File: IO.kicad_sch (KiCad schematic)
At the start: 12 parts, among them J2 Conn_Coaxial, J3 Conn_Coaxial, U6 ADG902BRMZ

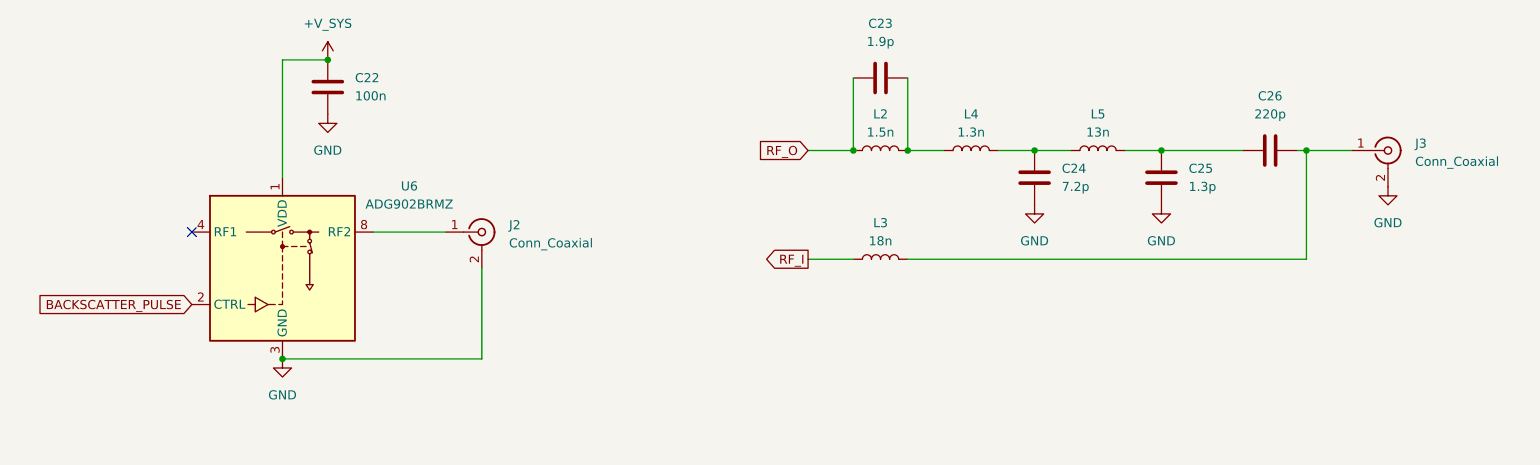
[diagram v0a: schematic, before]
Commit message: add IO ports, begin layout
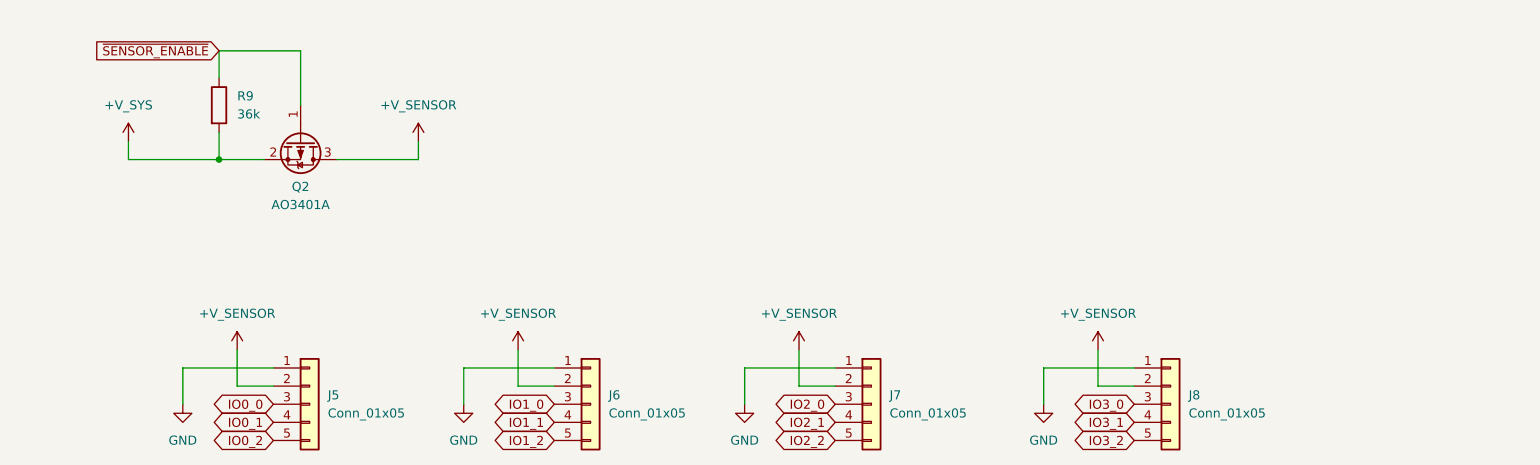
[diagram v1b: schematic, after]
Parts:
- removed C22: 100n, Capacitor_SMD:C_0603_1608Metric_Pad1.08x0.95mm_HandSolder, symbol Device:C
- removed C23: 1.9p, Capacitor_SMD:C_0603_1608Metric_Pad1.08x0.95mm_HandSolder, symbol Device:C
- removed C24: 7.2p, Capacitor_SMD:C_0603_1608Metric_Pad1.08x0.95mm_HandSolder, symbol Device:C
- removed C25: 1.3p, Capacitor_SMD:C_0603_1608Metric_Pad1.08x0.95mm_HandSolder, symbol Device:C
- removed C26: 220p, Capacitor_SMD:C_0603_1608Metric_Pad1.08x0.95mm_HandSolder, symbol Device:C
- removed J2, J3: Conn_Coaxial, Connector_Coaxial:SMA_Molex_73251-2200_Horizontal, symbol Connector:Conn_Coaxial
- removed L2: 1.5n, Inductor_SMD:L_0603_1608Metric_Pad1.05x0.95mm_HandSolder, symbol Device:L
- removed L3: 18n, Inductor_SMD:L_0603_1608Metric_Pad1.05x0.95mm_HandSolder, symbol Device:L
- removed L4: 1.3n, Inductor_SMD:L_0603_1608Metric_Pad1.05x0.95mm_HandSolder, symbol Device:L
- removed L5: 13n, Inductor_SMD:L_0603_1608Metric_Pad1.05x0.95mm_HandSolder, symbol Device:L
- removed U6: ADG902BRMZ, Package_SO:MSOP-8_3x3mm_P0.65mm, symbol RF_Switch:ADG902BRMZ
- added J5, J6, J7, J8: Conn_01x05, Connector_JST:JST_XH_B5B-XH-AM_1x05_P2.50mm_Vertical, symbol Connector_Generic:Conn_01x05
- added Q2: AO3401A, Package_TO_SOT_SMD:SOT-23, symbol Transistor_FET:AO3401A
- added R9: 36k, Resistor_SMD:R_0603_1608Metric_Pad0.98x0.95mm_HandSolder, symbol Device:R
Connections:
- net +V_SYS: now also Q2.2 (S), R9.2
- net GND: now also J5.1 (Pin_1), J6.1 (Pin_1), J7.1 (Pin_1), J8.1 (Pin_1)
- new net +V_SENSOR: J5.2 (Pin_2), J6.2 (Pin_2), J7.2 (Pin_2), J8.2 (Pin_2), Q2.3 (D)
- new net IO0_0: J5.3 (Pin_3)
- new net IO0_1: J5.4 (Pin_4)
- new net IO0_2: J5.5 (Pin_5)
- new net IO1_0: J6.3 (Pin_3)
- new net IO1_1: J6.4 (Pin_4)
- new net IO1_2: J6.5 (Pin_5)
- new net IO2_0: J7.3 (Pin_3)
- new net IO2_1: J7.4 (Pin_4)
- new net IO2_2: J7.5 (Pin_5)
- new net IO3_0: J8.3 (Pin_3)
- new net IO3_1: J8.4 (Pin_4)
- new net IO3_2: J8.5 (Pin_5)
- new net ~{SENSOR_ENABLE}: Q2.1 (G), R9.1
- no-connect marks 1 -> 0
